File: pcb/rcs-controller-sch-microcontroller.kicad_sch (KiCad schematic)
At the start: 46 parts, among them J4 Screw_Terminal_4_P3.50mm, J5 USB_C_Receptacle_USB2.0_14P, J6 Conn_01x03, Q2 SI7465DP-T1-E3, Q3 SI7465DP-T1-E3, Q4 PMV45EN2, Q5 PMV45EN2, Q6 DMP2045U, SW1 SW_Push, SW2 SW_Push, U1 LSM6DSOX, U4 ESP32-S3-WROOM-1, U5 AP2112K-3.3

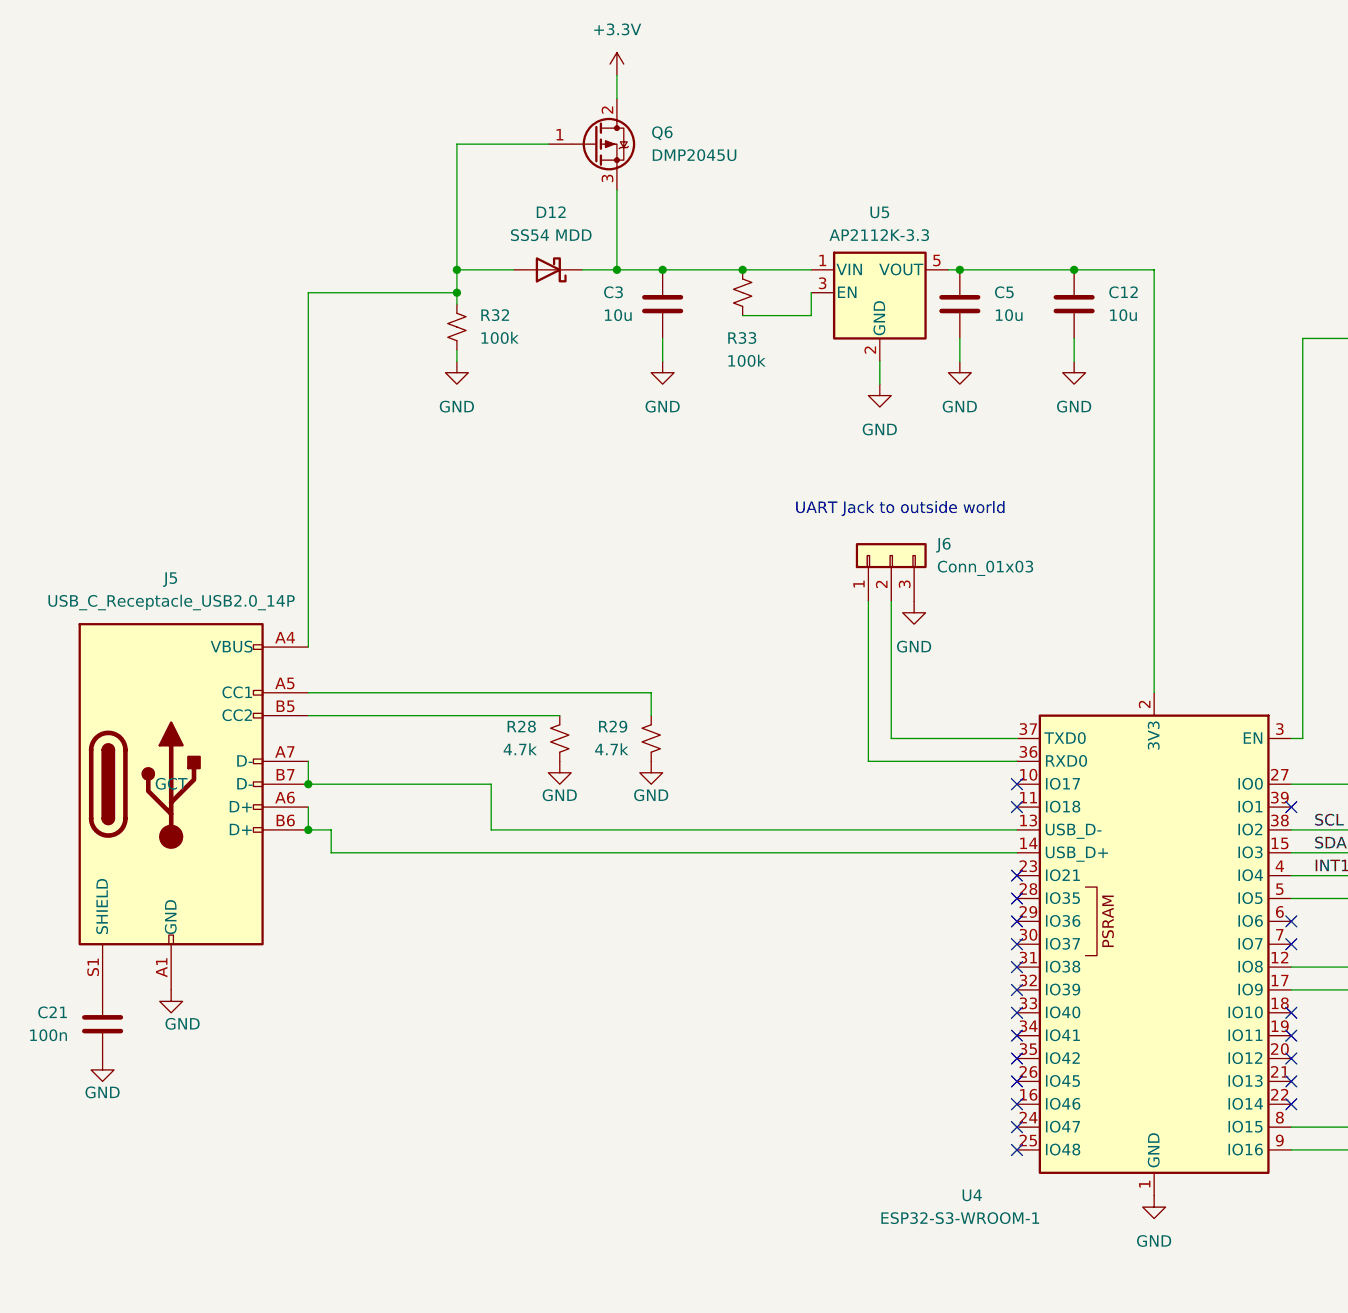
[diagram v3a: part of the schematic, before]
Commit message: power OR cleanup with Thomas for USB power
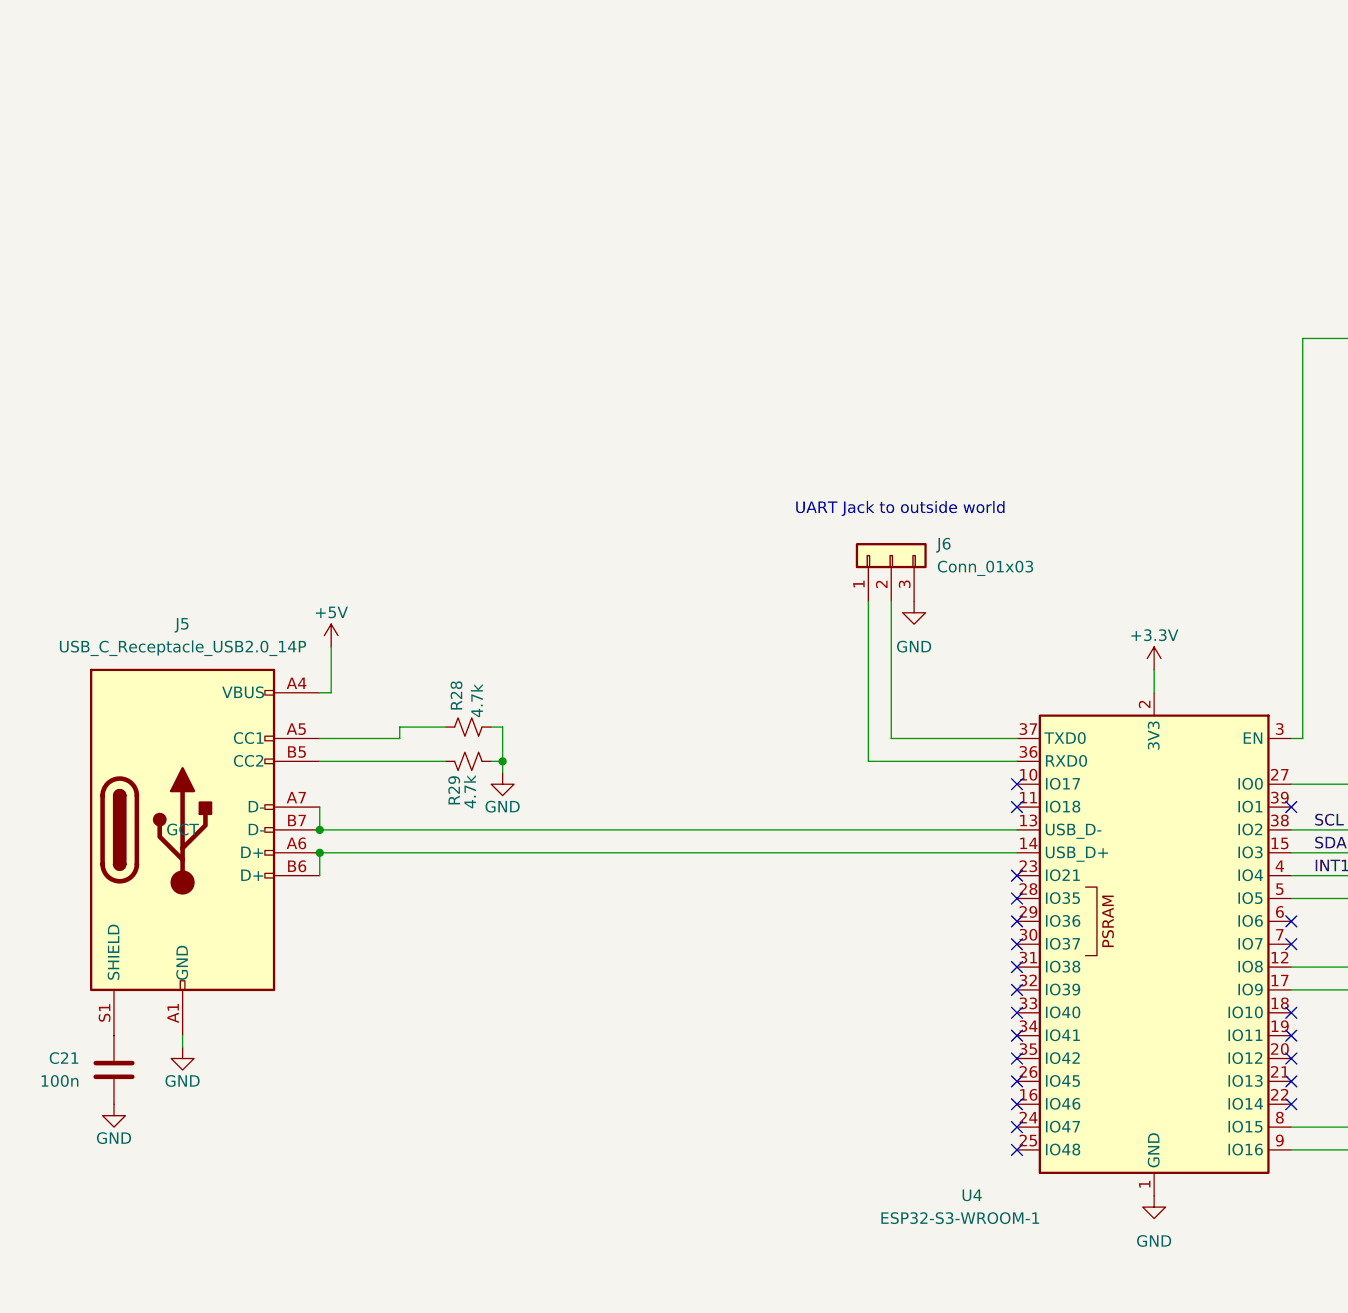
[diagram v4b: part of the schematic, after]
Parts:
- removed C12, C3, C5: 10u, symbol Device:C
- removed D12: SS54 MDD, symbol Device:D_Schottky
- removed Q6: DMP2045U, Package_TO_SOT_SMD:TO-252-2, symbol Transistor_FET:SUD08P06-155L
- removed R32, R33: 100k, symbol Device:R_Small_US
- removed U5: AP2112K-3.3, Package_TO_SOT_SMD:SOT-23-5, symbol Regulator_Linear:AP2112K-3.3
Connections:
- net +3.3V: now also U4.2 (3V3)
- net at R29.1: now also J5.B5 (CC2); no longer J5.A5 (CC1)
- net +5V: now reaches J5.A4 (VBUS), J5.A9 (VBUS), J5.B4 (VBUS), J5.B9 (VBUS)
- net at R28.1: now also J5.A5 (CC1); no longer J5.B5 (CC2)
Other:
- moved on the sheet: C21, J5, R28, R29

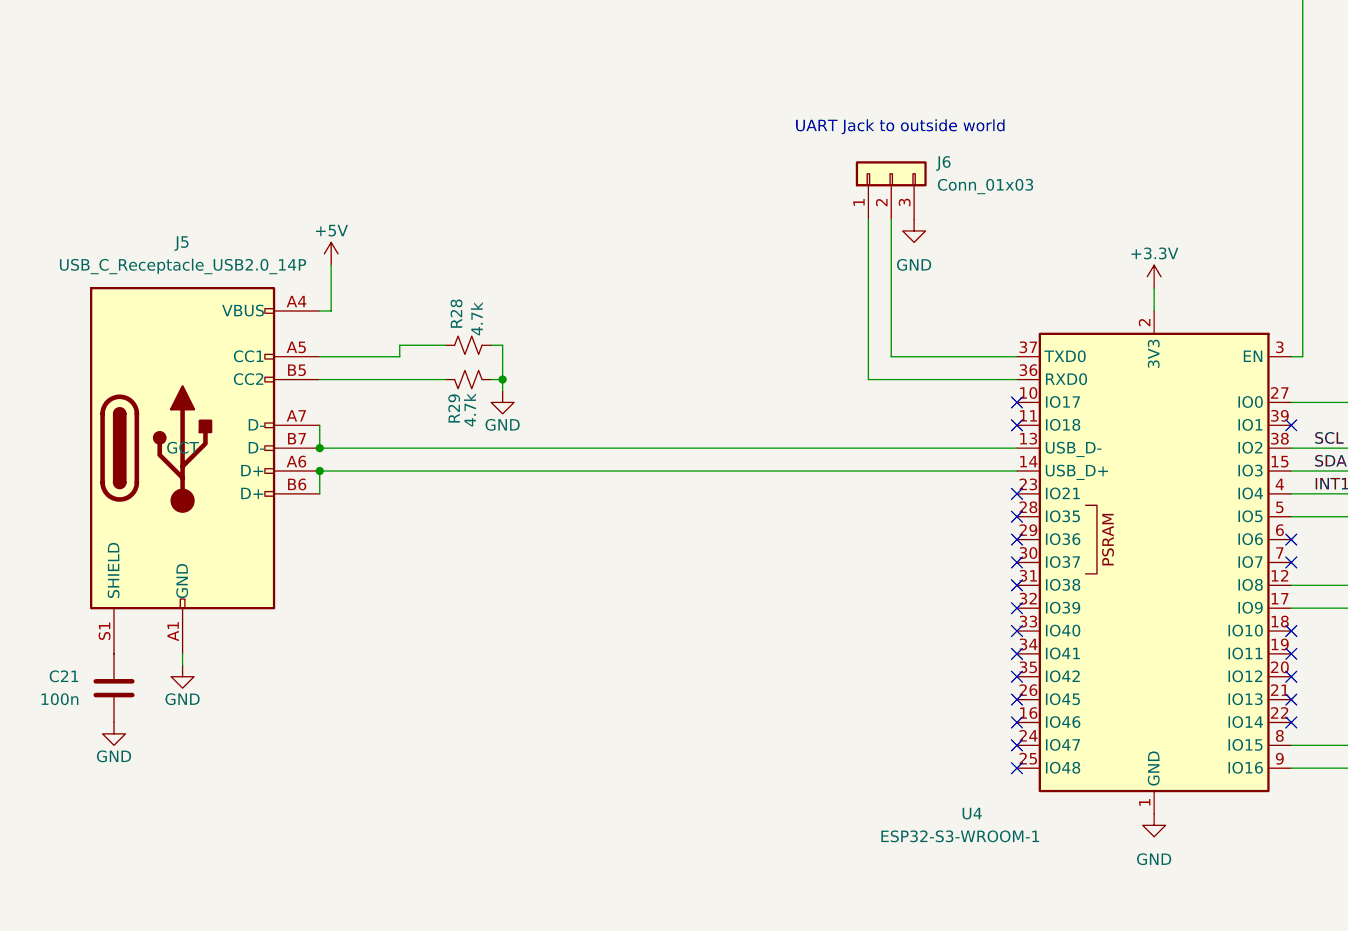
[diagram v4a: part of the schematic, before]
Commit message: Added Andrew's new power switching diode and removed some unconnected traces
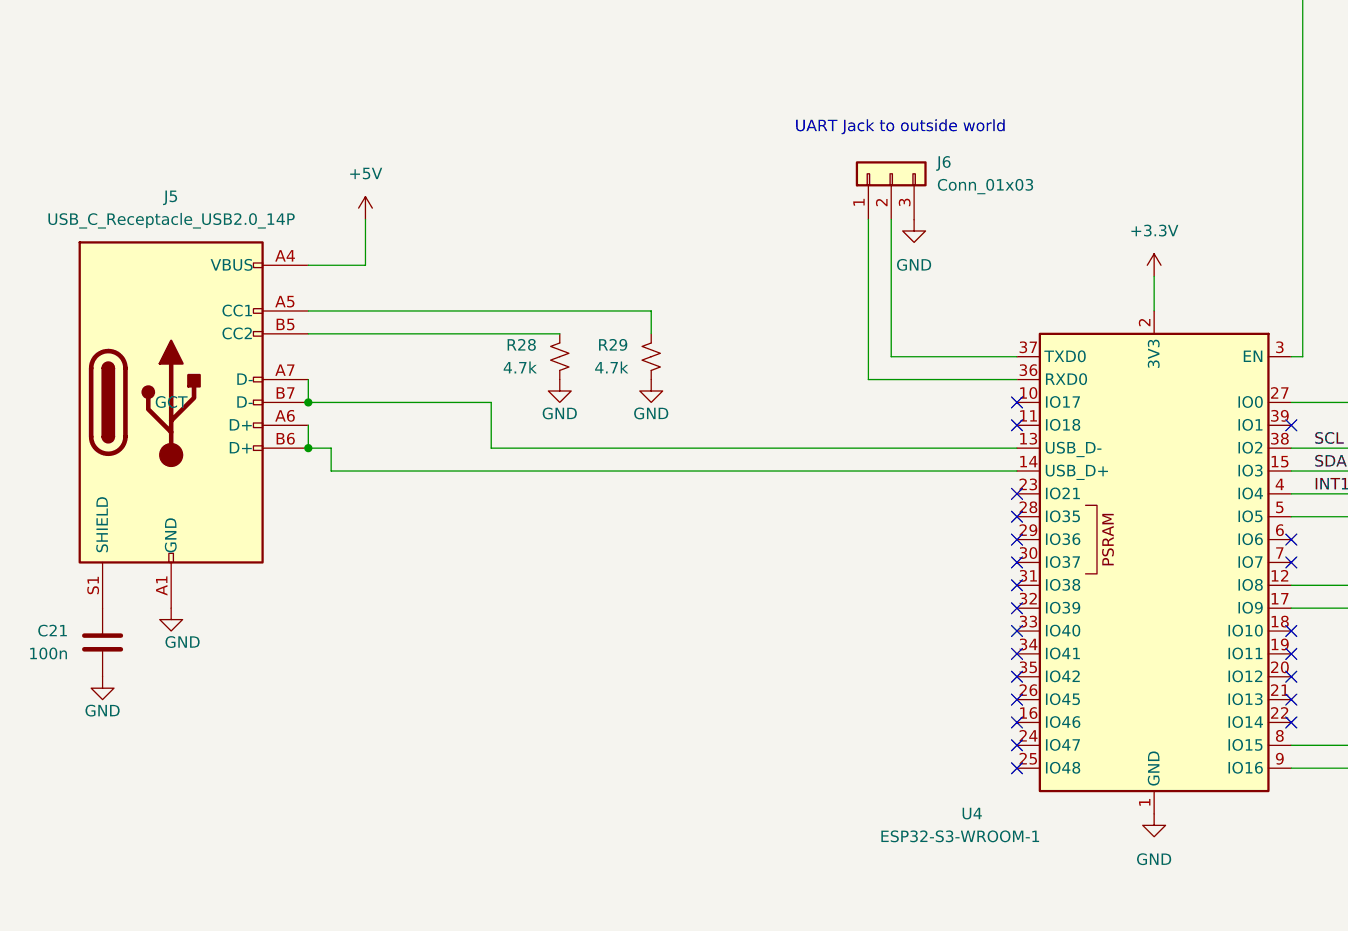
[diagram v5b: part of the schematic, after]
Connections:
- net at R29.1: now also J5.A5 (CC1); no longer J5.B5 (CC2)
- net at R28.1: now also J5.B5 (CC2); no longer J5.A5 (CC1)
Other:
- moved on the sheet: C21, J5, R28, R29

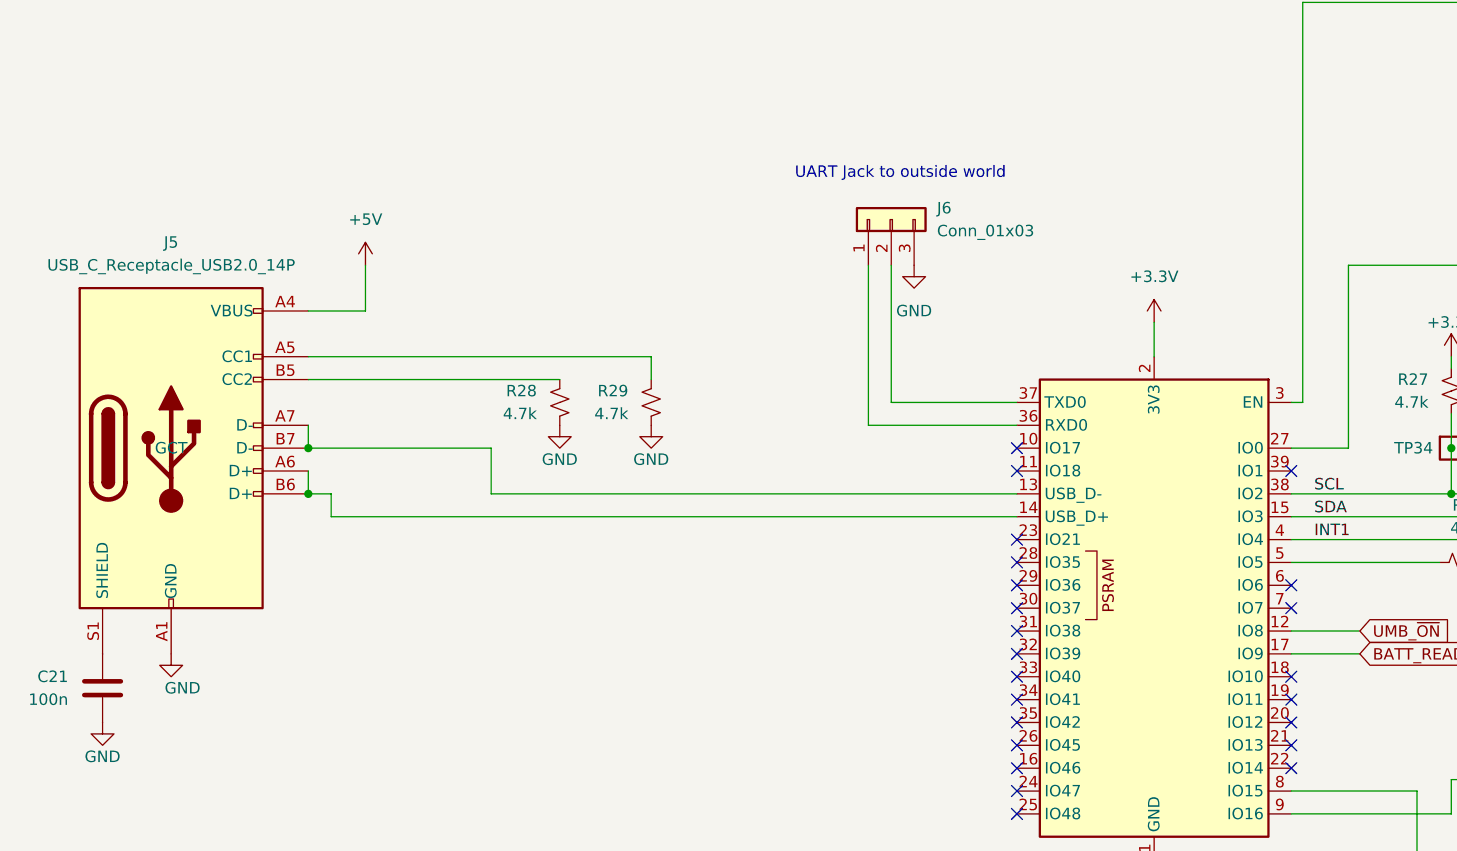
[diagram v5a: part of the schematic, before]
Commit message: Added ports to transducer and power switch
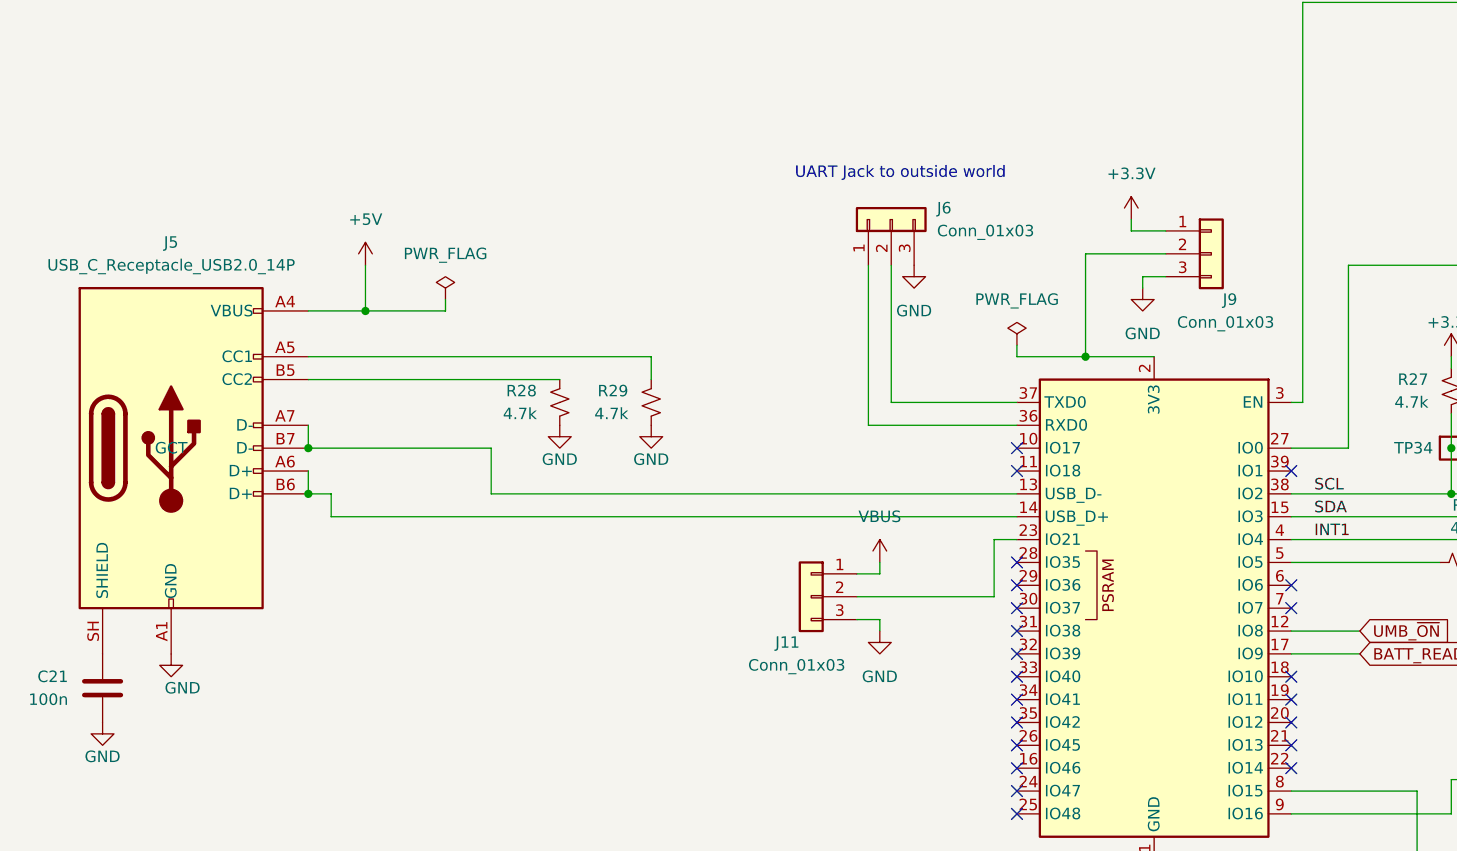
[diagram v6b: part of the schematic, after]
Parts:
- added J11, J9: Conn_01x03, Connector_Molex:Molex_KK-254_AE-6410-03A_1x03_P2.54mm_Vertical, symbol Connector_Generic:Conn_01x03
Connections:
- net +3.3V: now also J9.1 (Pin_1); no longer U4.2 (3V3)
- net GND: now also J11.3 (Pin_3), J9.3 (Pin_3)
- net VBUS: now also J11.1 (Pin_1)
- net at C21.1: now also J5.SH (SHIELD); no longer J5.S1 (SHIELD)
- net at U4.23 (IO21): now also J11.2 (Pin_2)
- new net: J9.2 (Pin_2), U4.2 (3V3)
- no-connect marks 26 -> 25
